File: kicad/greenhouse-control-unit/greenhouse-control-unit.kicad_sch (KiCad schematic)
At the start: 68 parts, among them J1 Pluggable_Terminal_01x02, J10 Conn_01x15_Female, J10_LittleBuck1 Conn_01x01_Female, J11 Molex_KK-254_01x03, J11_LittleBuck1 Conn_01x01_Female, J12 Molex_KK-396_01x16, J12_BigBuck1 Conn_01x01_Female, J13 Molex_KK-254_01x10, J13_BigBuck1 Conn_01x01_Female, J14 Molex_KK-254_01x02, J14_LittleBuck1 Conn_01x01_Female, J15_LittleBuck1 Conn_01x01_Female, J2 Pluggable_Terminal_01x02, J3 Pluggable_Terminal_01x02, J4 Molex_KK-254_01x02, J5 Molex_KK-254_01x03, J6 Molex_KK-254_01x02, J6_BigBuck1 Conn_01x01_Female, J7 Conn_01x10_Female, J7_BigBuck1 Conn_01x01_Female, J8 Conn_01x10_Female, J9 Conn_01x15_Female, Q1 2N7000, Q10 IRLB8721PBF, Q11 IRLB8721PBF, Q12 IRLB8721PBF, Q13 IRLB8721PBF, Q2 2N7000, Q3 2N7000, Q4 IRLB8721PBF, Q5 IRLB8721PBF, Q6 IRLB8721PBF, Q7 IRLB8721PBF, Q8 2N7000, Q9 2N7000, U1 74HC595, U2 74HC595

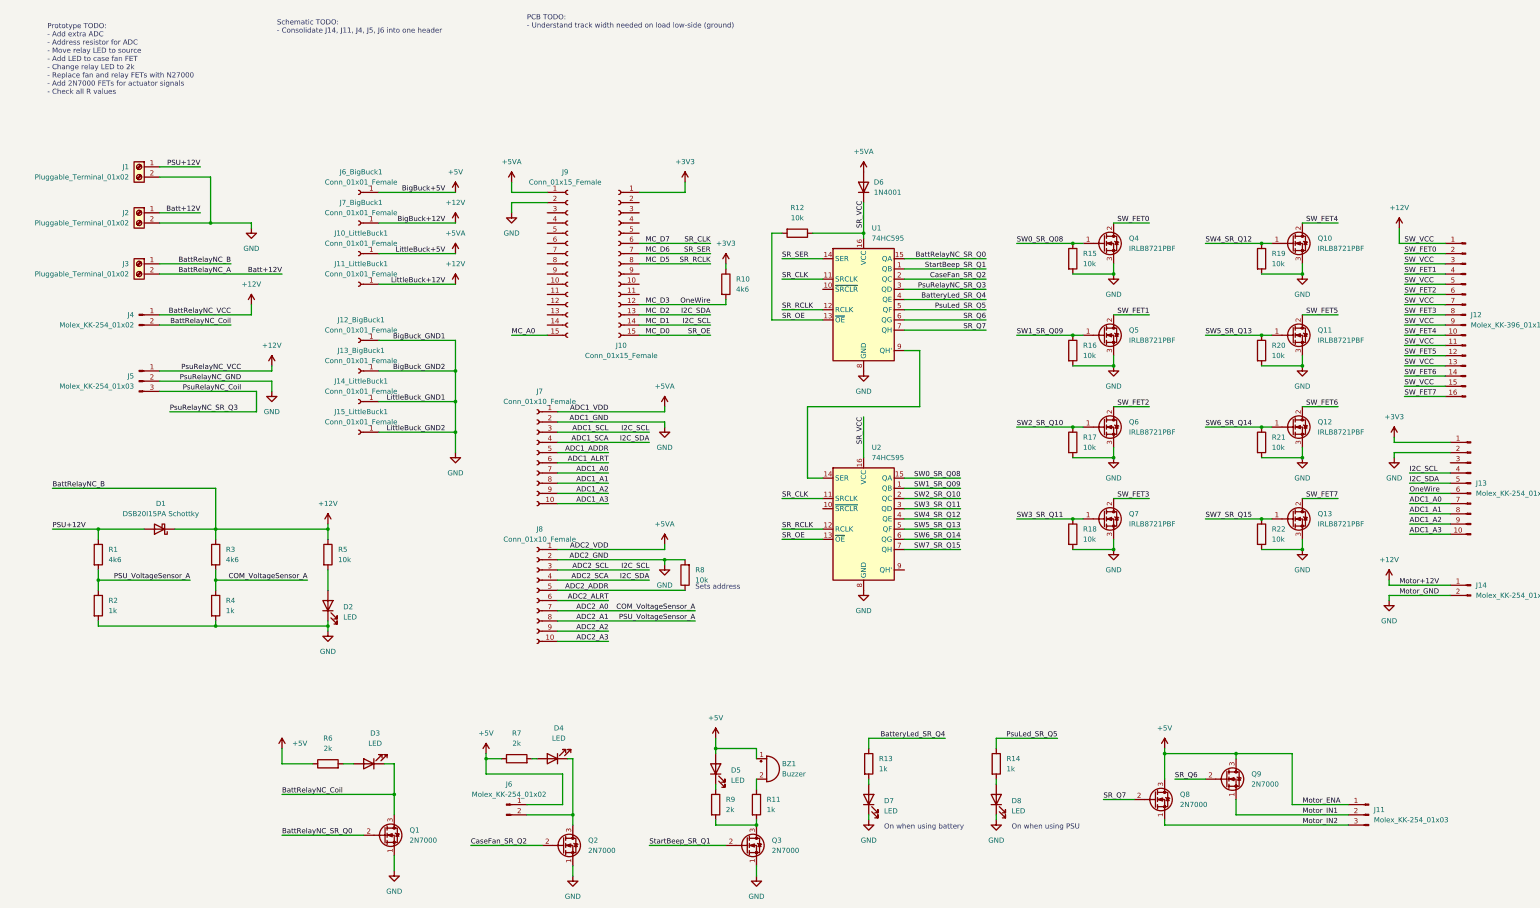
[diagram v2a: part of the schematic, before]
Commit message: Caps to SR VCC, tie SRCLR to GND
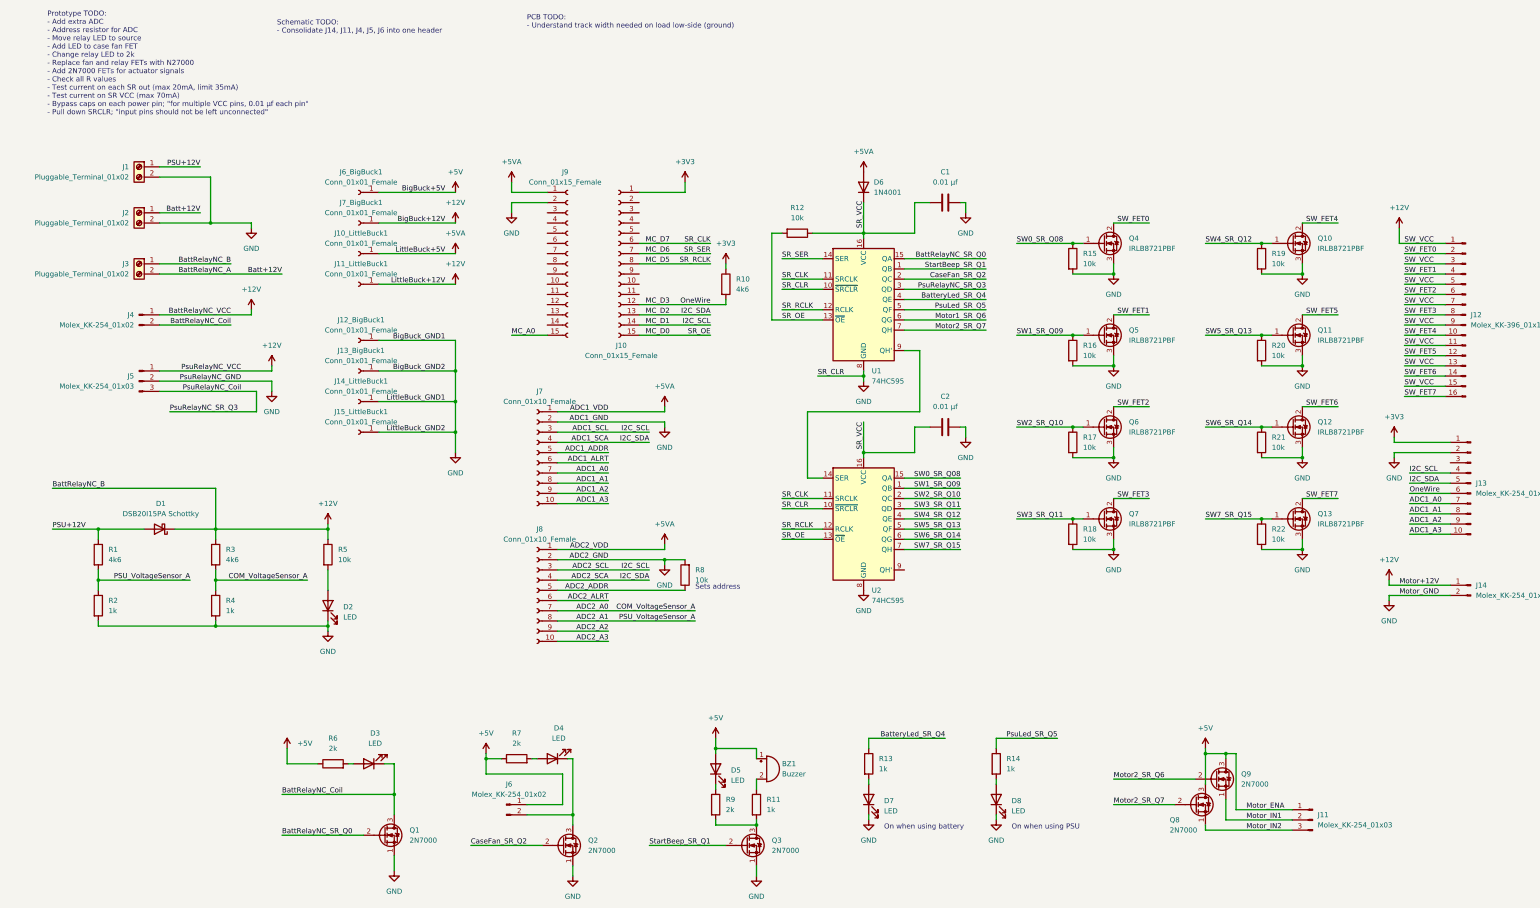
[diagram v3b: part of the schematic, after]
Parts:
- added C1, C2: 0.01 μf, symbol Device:C
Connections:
- net GND: now also U1.10 (~{SRCLR}), U2.10 (~{SRCLR}), C1.2, C2.2
- net SR_VCC: now also C1.1, C2.1
- net SR_Q6 renamed Motor1_SR_Q6
- net Motor1_SR_Q6: no longer Q9.2 (G)
- net SR_Q7 renamed Motor2_SR_Q7
- new net Motor2_SR_Q6: Q9.2 (G)
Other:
- note added: "Prototype TODO: - Add extra ADC - Address resistor for ADC - Move relay LED to source - Add LED to case fan FET - Change relay LED to 2k - Replace fan and relay FETs with N27000 - Add 2N7000 FETs for actuator signals - Check all R values - Test current on each SR out (max 20mA, limit 35mA) - Test current on SR VCC (max 70mA) - Bypass caps on each power pin; "for multiple VCC pins, 0.01 μf each pi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"
- note removed: "Prototype TODO: - Add extra ADC - Address resistor for ADC - Move relay LED to source - Add LED to case fan FET - Change relay LED to 2k - Replace fan and relay FETs with N27000 - Add 2N7000 FETs for actuator signals - Check all R values"
- moved on the sheet: J11, Q8, Q9, R6

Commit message: Consolidate KK headers, connect all traces on PCB
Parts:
- removed J11, J5: Molex_KK-254_01x03, Connector_Molex:Molex_KK-254_AE-6410-03A_1x03_P2.54mm_Vertical, symbol Connector:Conn_01x03_Male
- removed J14, J4, J6: Molex_KK-254_01x02, Connector_Molex:Molex_KK-254_AE-6410-02A_1x02_P2.54mm_Vertical, symbol Connector:Conn_01x02_Male
- added J4: Molex_KK-254_01x08, Connector_Molex:Molex_KK-254_AE-6410-08A_1x08_P2.54mm_Vertical, symbol Connector:Conn_01x08_Male
- C1, C2: footprint (none) -> Capacitor_THT:C_Disc_D3.0mm_W1.6mm_P2.50mm
- R10: renamed from R12; footprint Resistor_THT:R_Axial_DIN0207_L6.3mm_D2.5mm_P7.62mm_Horizontal -> Resistor_THT:R_Axial_DIN0204_L3.6mm_D1.6mm_P5.08mm_Horizontal
- R8: footprint Resistor_THT:R_Axial_DIN0207_L6.3mm_D2.5mm_P7.62mm_Horizontal -> Resistor_THT:R_Axial_DIN0204_L3.6mm_D1.6mm_P5.08mm_Horizontal
- renumbered J13 to J10, J7 to J5, J8 to J6, J9 to J7, J10 to J8, J12 to J9, Q12 to Q10, Q13 to Q11, Q8 to Q12, Q9 to Q13, Q10 to Q8, Q11 to Q9, R9 to R11, R11 to R12, R15 to R14, R16 to R15, R17 to R16, R18 to R17, R14 to R18, R10 to R9
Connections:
- net Motor2_SR_Q6 is gone; now on net Motor1_SR_Q6: Q13.2 (G)
- net +12V: now also J4.1 (Pin_1)
- net +3V3: now also J5.1 (Pin_1), J6.1 (Pin_1)
- net +5V: now also J4.2 (Pin_2)
- net +5VA: no longer J5.1 (Pin_1), J6.1 (Pin_1)
- net BattRelayNC_Coil: now also J4.4 (Pin_4)
- net GND: now also J4.3 (Pin_3)
- net Motor_IN1: now also J4.8 (Pin_8)
- net Motor_IN2: now also J4.7 (Pin_7)
- net PsuRelayNC_Coil: now also J4.5 (Pin_5)
- net CaseFan_FET: now reaches D4.1 (K), Q2.3 (D)
- net CaseFan_FET: now also J4.6 (Pin_6)
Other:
- note added: "PCB TODO: -"
- note added: "Schematic TODO: -"
- note removed: "PCB TODO: - Understand track width needed on load low-side (ground)"
- note removed: "Schematic TODO: - Consolidate J14, J11, J4, J5, J6 into one header"
- moved on the sheet: BZ1, D1, D2, D3, D5, D7, D8, Q1, Q12, Q13, Q2, Q3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

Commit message: Add mounting holes
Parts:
- added H1, H2, H3, H4, H5, H6: MountingHole, MountingHole:MountingHole_3mm, symbol Mechanical:MountingHole
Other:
- title: (none) -> Greenhouse control unit
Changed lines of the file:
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@@
 (kicad_sch (version 20211123) (generator eeschema)
   (paper "A3")
+  (title_block
+    (title "Greenhouse control unit")
+    (date "2022-03-27")
+    (rev "1")
+  )
   (junction (at 104.14 180.34) (diameter 0) (color 0 0 0 0)
   )
@@
     (pin "2")
   )
+  (symbol (lib_id "Mechanical:MountingHole") (at 365.76 35.56 0) (unit 1)
+    (in_bom yes) (on_board yes) (fields_autoplaced)
+    (property "Reference" "H3" (id 0) (at 368.3 34.2899 0)
+      (effects (font (size 1.27 1.27)) (justify left))
+    )
+    (property "Value" "MountingHole" (id 1) (at 368.3 36.8299 0)
+      (effects (font (size 1.27 1.27)) (justify left))
+    )
+    (property "Footprint" "MountingHole:MountingHole_3mm" (id 2) (at 365.76 35.56 0)
+      (effects (font (size 1.27 1.27)) hide)
+    )
+    (property "Datasheet" "~" (id 3) (at 365.76 35.56 0)
+      (effects (font (size 1.27 1.27)) hide)
+    )
+  )
   (symbol (lib_id "power:GND") (at 342.9 105.41 0) (unit 1)
     (in_bom yes) (on_board yes) (fields_autoplaced)
@@
     (pin "1")
   )
+  (symbol (lib_id "Mechanical:MountingHole") (at 365.76 50.8 0) (unit 1)
+    (in_bom yes) (on_board yes) (fields_autoplaced)
+    (property "Reference" "H6" (id 0) (at 368.3 49.5299 0)
+      (effects (font (size 1.27 1.27)) (justify left))
+    )
+    (property "Value" "MountingHole" (id 1) (at 368.3 52.0699 0)
+      (effects (font (size 1.27 1.27)) (justify left))
+    )
+    (property "Footprint" "MountingHole:MountingHole_3mm" (id 2) (at 365.76 50.8 0)
+      (effects (font (size 1.27 1.27)) hide)
+    )
+    (property "Datasheet" "~" (id 3) (at 365.76 50.8 0)
+      (effects (font (size 1.27 1.27)) hide)
+    )
+  )
   (symbol (lib_id "Transistor_FET:2N7000") (at 185.42 233.68 0) (unit 1)
     (in_bom yes) (on_board yes) (fields_autoplaced)
@@
     (pin "9")
   )
+  (symbol (lib_id "Mechanical:MountingHole") (at 365.76 30.48 0) (unit 1)
+    (in_bom yes) (on_board yes) (fields_autoplaced)
+    (property "Reference" "H2" (id 0) (at 368.3 29.2099 0)
+      (effects (font (size 1.27 1.27)) (justify left))
+    )
+    (property "Value" "MountingHole" (id 1) (at 368.3 31.7499 0)
+      (effects (font (size 1.27 1.27)) (justify left))
+    )
+    (property "Footprint" "MountingHole:MountingHole_3mm" (id 2) (at 365.76 30.48 0)
+      (effects (font (size 1.27 1.27)) hide)
+    )
+    (property "Datasheet" "~" (id 3) (at 365.76 30.48 0)
+      (effects (font (size 1.27 1.27)) hide)
+    )
+  )
   (symbol (lib_id "power:+3V3") (at 365.76 123.19 0) (unit 1)
     (in_bom yes) (on_board yes) (fields_autoplaced)
@@
     (pin "9")
   )
+  (symbol (lib_id "Mechanical:MountingHole") (at 365.76 40.64 0) (unit 1)
+    (in_bom yes) (on_board yes) (fields_autoplaced)
+    (property "Reference" "H4" (id 0) (at 368.3 39.3699 0)
+      (effects (font (size 1.27 1.27)) (justify left))
+    )
+    (property "Value" "MountingHole" (id 1) (at 368.3 41.9099 0)
+      (effects (font (size 1.27 1.27)) (justify left))
+    )
+    (property "Footprint" "MountingHole:MountingHole_3mm" (id 2) (at 365.76 40.64 0)
+      (effects (font (size 1.27 1.27)) hide)
+    )
+    (property "Datasheet" "~" (id 3) (at 365.76 40.64 0)
+      (effects (font (size 1.27 1.27)) hide)
+    )
+  )
   (symbol (lib_id "power:+5V") (at 120.65 217.17 0) (unit 1)
     (in_bom yes) (on_board yes) (fields_autoplaced)
@@
     (pin "1")
   )
+  (symbol (lib_id "Mechanical:MountingHole") (at 365.76 45.72 0) (unit 1)
+    (in_bom yes) (on_board yes) (fields_autoplaced)
+    (property "Reference" "H5" (id 0) (at 368.3 44.4499 0)
+      (effects (font (size 1.27 1.27)) (justify left))
+    )
+    (property "Value" "MountingHole" (id 1) (at 368.3 46.9899 0)
+      (effects (font (size 1.27 1.27)) (justify left))
+    )
+    (property "Footprint" "MountingHole:MountingHole_3mm" (id 2) (at 365.76 45.72 0)
+      (effects (font (size 1.27 1.27)) hide)
+    )
+    (property "Datasheet" "~" (id 3) (at 365.76 45.72 0)
+      (effects (font (size 1.27 1.27)) hide)
+    )
+  )
   (symbol (lib_id "Connector:Conn_01x08_Male") (at 86.36 148.59 0) (unit 1)
     (in_bom yes) (on_board yes) (fields_autoplaced)
@@
     (pin "2")
   )
+  (symbol (lib_id "Mechanical:MountingHole") (at 365.76 25.4 0) (unit 1)
+    (in_bom yes) (on_board yes) (fields_autoplaced)
+    (property "Reference" "H1" (id 0) (at 368.3 24.1299 0)
+      (effects (font (size 1.27 1.27)) (justify left))
+    )
+    (property "Value" "MountingHole" (id 1) (at 368.3 26.6699 0)
+      (effects (font (size 1.27 1.27)) (justify left))
+    )
+    (property "Footprint" "MountingHole:MountingHole_3mm" (id 2) (at 365.76 25.4 0)
+      (effects (font (size 1.27 1.27)) hide)
+    )
+    (property "Datasheet" "~" (id 3) (at 365.76 25.4 0)
+      (effects (font (size 1.27 1.27)) hide)
+    )
+  )
   (symbol (lib_id "Transistor_FET:IRLB8721PBF") (at 340.36 74.93 0) (unit 1)
     (in_bom yes) (on_board yes) (fields_autoplaced)
@@
       (reference "D8") (unit 1) (value "LED") (footprint "LED_THT:LED_D5.0mm")
     )
+    (path "/e0ff723e-9da4-419a-9b7c-537137a1c661"
+      (reference "H1") (unit 1) (value "MountingHole") (footprint "MountingHole:MountingHole_3mm")
+    )
+    (path "/1defaa8a-584e-44e7-a824-f4a42cf2ea56"
+      (reference "H2") (unit 1) (value "MountingHole") (footprint "MountingHole:MountingHole_3mm")
+    )
+    (path "/09d94f95-f953-476f-83e3-f1c6db04e6b4"
+      (reference "H3") (unit 1) (value "MountingHole") (footprint "MountingHole:MountingHole_3mm")
+    )
+    (path "/26ab1162-16d0-49df-8ca5-5a6a1be3d60b"
+      (reference "H4") (unit 1) (value "MountingHole") (footprint "MountingHole:MountingHole_3mm")
+    )
+    (path "/92cb044d-0d05-4bb8-9560-1ba1b1cb2197"
+      (reference "H5") (unit 1) (value "MountingHole") (footprint "MountingHole:MountingHole_3mm")
+    )
+    (path "/177c16ad-cbf7-4800-8d46-4d4c6848fdbe"
+      (reference "H6") (unit 1) (value "MountingHole") (footprint "MountingHole:MountingHole_3mm")
+    )
     (path "/2bcf145a-d9ab-4e76-b5a5-d44e828f07e3"
